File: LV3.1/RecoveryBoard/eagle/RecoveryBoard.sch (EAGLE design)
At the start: 90 parts, among them IC1 BD62120AEFJ-E2, Q6 MOSFET-PCH-SOT23-6, U1 STM32F042K6, U10 TPS63070, Y1 ECS-160-10-36Q-ES-TR

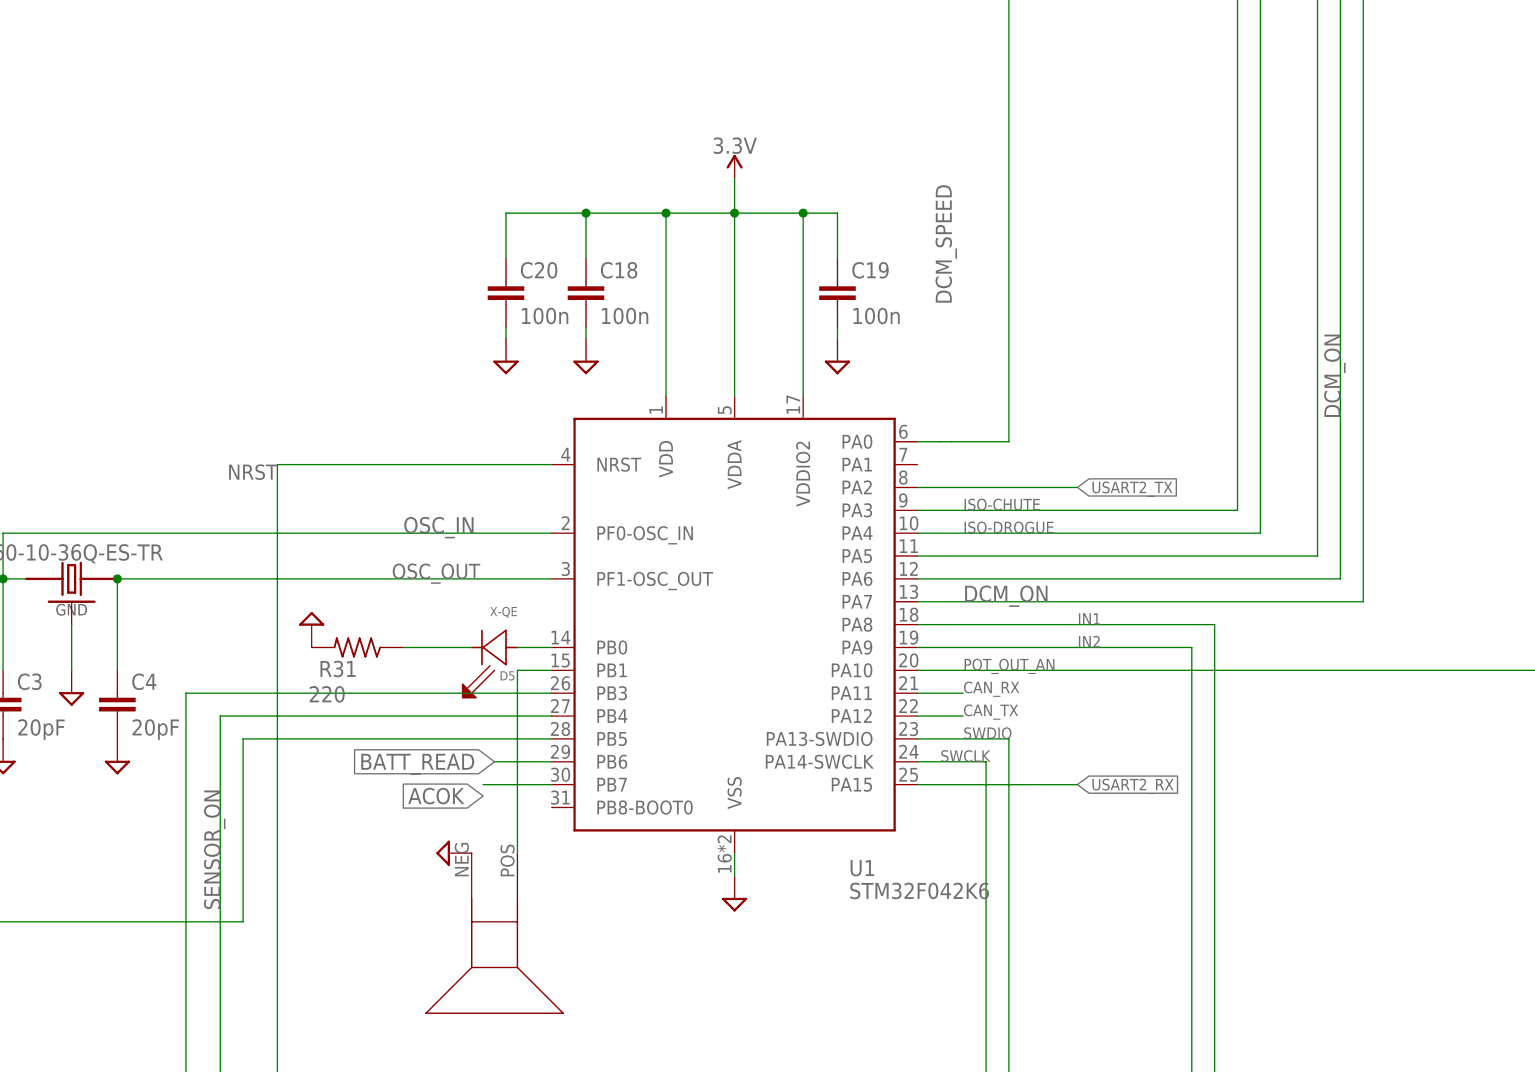
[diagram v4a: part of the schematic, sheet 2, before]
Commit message: finished routing and added TODO list
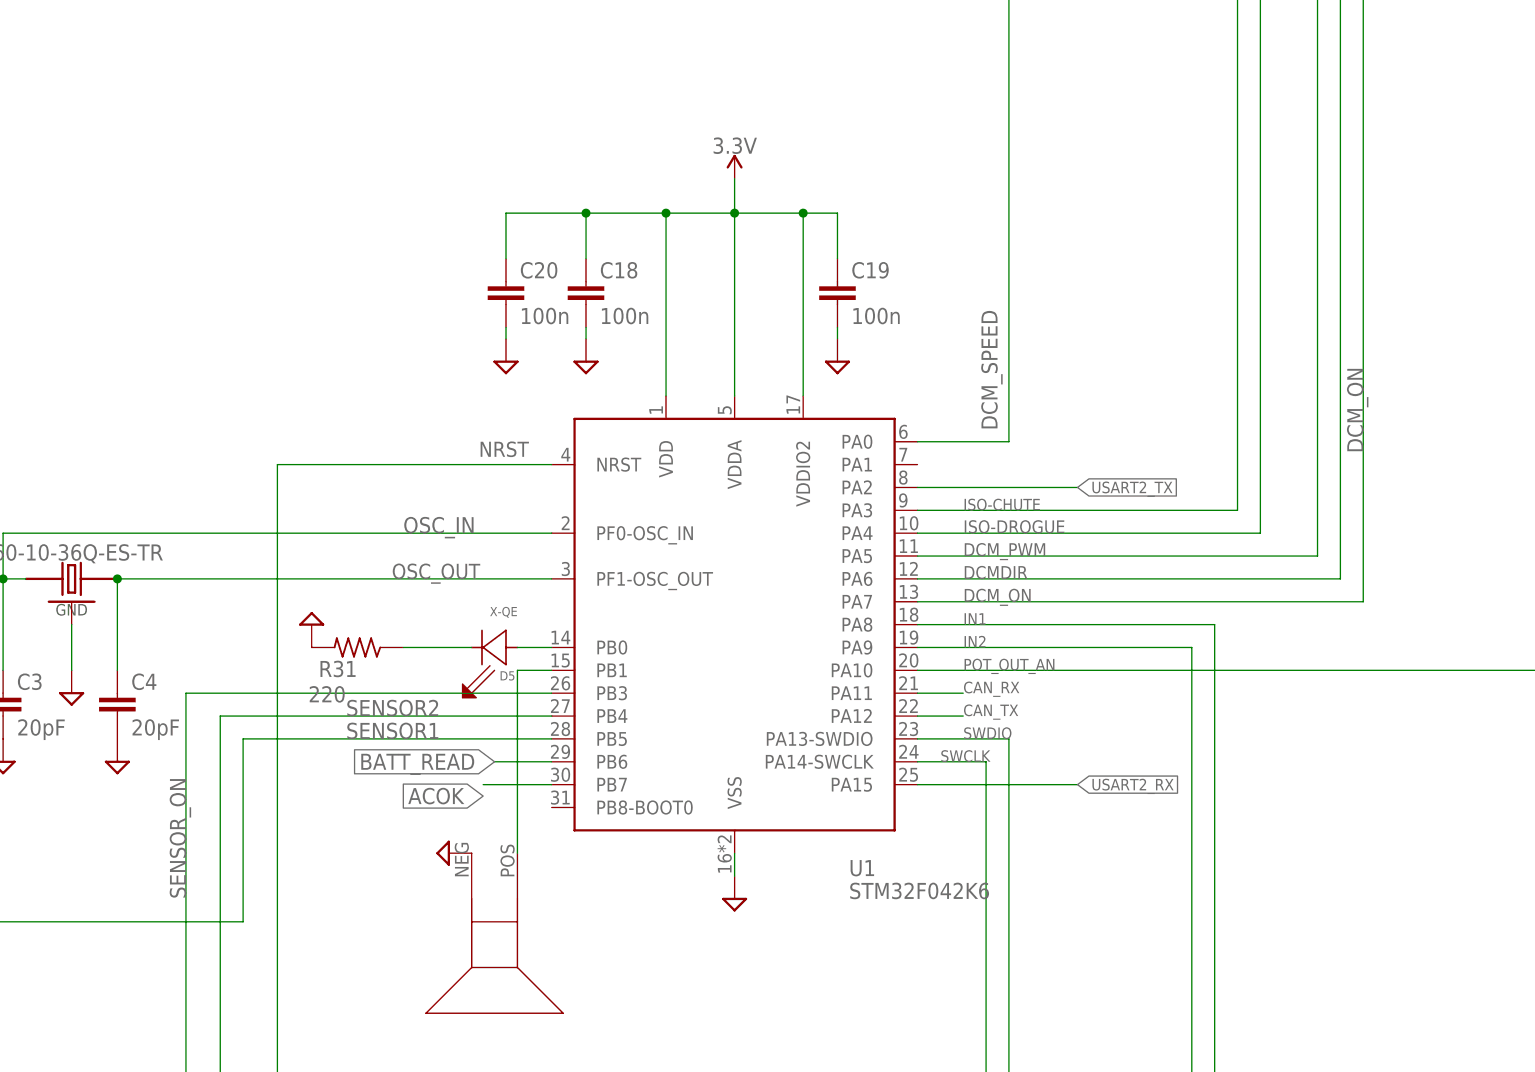
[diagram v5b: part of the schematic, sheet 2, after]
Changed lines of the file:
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@@
 <pinref part="U1" gate="G$1" pin="PA8"/>
 <wire x1="294.64" y1="185.42" x2="327.66" y2="185.42" width="0.1524" layer="91"/>
-<label x="312.42" y="185.42" size="1.27" layer="95"/>
+<label x="299.72" y="185.42" size="1.27" layer="95"/>
 <pinref part="R32" gate="R" pin="1"/>
 <junction x="386.08" y="118.11"/>
@@
 <pinref part="U1" gate="G$1" pin="PA9"/>
 <wire x1="294.64" y1="182.88" x2="325.12" y2="182.88" width="0.1524" layer="91"/>
-<label x="312.42" y="182.88" size="1.27" layer="95"/>
+<label x="299.72" y="182.88" size="1.27" layer="95"/>
 <wire x1="325.12" y1="182.88" x2="325.12" y2="134.62" width="0.1524" layer="91"/>
 <wire x1="325.12" y1="134.62" x2="386.08" y2="134.62" width="0.1524" layer="91"/>
@@
 <wire x1="219.71" y1="172.72" x2="219.71" y2="152.4" width="0.1524" layer="91"/>
 <wire x1="219.71" y1="172.72" x2="254" y2="172.72" width="0.1524" layer="91"/>
+<label x="231.14" y="172.72" size="1.778" layer="95"/>
 </segment>
 </net>
@@
 <pinref part="U1" gate="G$1" pin="NRST"/>
 <wire x1="254" y1="203.2" x2="223.52" y2="203.2" width="0.1524" layer="91"/>
-<label x="223.52" y="203.2" size="1.6764" layer="95" rot="R180"/>
+<label x="251.46" y="205.74" size="1.6764" layer="95" rot="R180"/>
 <pinref part="CM1" gate="A" pin="!RESET"/>
 <label x="251.46" y="48.26" size="1.6764" layer="95" rot="R180"/>
@@
 <pinref part="U1" gate="G$1" pin="PA6"/>
 <wire x1="294.64" y1="190.5" x2="341.63" y2="190.5" width="0.1524" layer="91"/>
+<label x="299.72" y="190.5" size="1.4224" layer="95"/>
 </segment>
 </net>
@@
 <wire x1="88.9" y1="95.25" x2="91.44" y2="95.25" width="0.1524" layer="91"/>
 <junction x="88.9" y="95.25"/>
-<label x="217.17" y="153.67" size="1.778" layer="95" rot="R90"/>
 <label x="130.81" y="76.2" size="1.778" layer="95"/>
 <pinref part="U1" gate="G$1" pin="PB3"/>
 <wire x1="213.36" y1="177.8" x2="254" y2="177.8" width="0.1524" layer="91"/>
+<label x="213.36" y="154.94" size="1.778" layer="95" rot="R90"/>
 </segment>
 </net>
@@
 <pinref part="U1" gate="G$1" pin="PB4"/>
 <wire x1="254" y1="175.26" x2="217.17" y2="175.26" width="0.1524" layer="91"/>
+<label x="231.14" y="175.26" size="1.778" layer="95"/>
 </segment>
 </net>
@@
 <wire x1="339.09" y1="193.04" x2="339.09" y2="269.24" width="0.1524" layer="91"/>
 <wire x1="339.09" y1="193.04" x2="294.64" y2="193.04" width="0.1524" layer="91"/>
+<label x="299.72" y="193.04" size="1.4224" layer="95"/>
 </segment>
 </net>
@@
 <wire x1="387.35" y1="261.62" x2="344.17" y2="261.62" width="0.1524" layer="91"/>
 <junction x="393.7" y="312.42"/>
-<label x="341.63" y="208.28" size="1.778" layer="95" rot="R90"/>
+<label x="344.17" y="204.47" size="1.778" layer="95" rot="R90"/>
 <wire x1="344.17" y1="261.62" x2="344.17" y2="187.96" width="0.1524" layer="91"/>
 <pinref part="U1" gate="G$1" pin="PA7"/>
-<label x="299.72" y="187.96" size="1.778" layer="95"/>
+<label x="299.72" y="187.96" size="1.4224" layer="95"/>
 <wire x1="294.64" y1="187.96" x2="344.17" y2="187.96" width="0.1524" layer="91"/>
 </segment>
@@
 <junction x="459.74" y="275.59"/>
 <pinref part="U1" gate="G$1" pin="PA0"/>
-<wire x1="298.45" y1="205.74" x2="297.18" y2="205.74" width="0.1524" layer="91"/>
-<label x="298.45" y="220.98" size="1.778" layer="95" rot="R90"/>
-<wire x1="297.18" y1="205.74" x2="294.64" y2="205.74" width="0.1524" layer="91"/>
+<label x="303.53" y="207.01" size="1.778" layer="95" rot="R90"/>
 <wire x1="304.8" y1="264.16" x2="304.8" y2="205.74" width="0.1524" layer="91"/>
-<wire x1="304.8" y1="205.74" x2="298.45" y2="205.74" width="0.1524" layer="91"/>
+<wire x1="304.8" y1="205.74" x2="294.64" y2="205.74" width="0.1524" layer="91"/>
 </segment>
 </net>
@@
 <net name="ISO-DROGUE" class="0">
 <segment>
-<label x="299.72" y="195.58" size="1.27" layer="95"/>
+<label x="299.72" y="195.58" size="1.4224" layer="95"/>
 <wire x1="332.74" y1="195.58" x2="332.74" y2="311.15" width="0.1524" layer="91"/>
 <wire x1="270.51" y1="311.15" x2="332.74" y2="311.15" width="0.1524" layer="91"/>

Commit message: More destruction on Ben's nice board. Good job Ben for putting up with Andrew.
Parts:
- removed U$1, U$2: NCH-SOT223, Q-MOSFET-NCH-SOT223:NCH-SOT223
- added Q1, Q2, Q3: BSS123, transistor-small-signal:BSS123
- added R37: 10k, oresat-rcl:R-US_0603-C-NOSILK
- D3, D4, D5: value X-QE -> (none); device D-Cree-XQE-LED:X-QE -> led:LEDCHIPLED_0603
- R18, R30: value (none) -> 1k
- R31: value 220 -> 1k
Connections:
- net N$9 renamed !BEN
- new net N$1: Q1.D, U$7.NEG
- net 3.3V: now also U$7.POS
- net DCM_ON: now also Q3.G; no longer U$1.G
- net GND: now also IC1.EP, Q1.S, Q2.S, Q3.S, R37.2; no longer U$1.S, U$2.S, U$7.NEG
- net N$27: now also Q2.D; no longer U$2.D
- net N$6: now also Q3.D; no longer U$1.D
- net N$8: now also Q1.G, R37.1; no longer U$7.POS
- net SENSOR_ON: now also Q2.G; no longer U$2.G
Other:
- note added: "From Telemetrum"
- note removed: "Do we still need an Arm input? there is no state where the board has power and is disarmed...this would free up a pin for a lock button"
- note removed: "Motor Control"
- moved on the sheet: C11, C12, C13, C14, C15, C16, C17, C21, D1, D2, JP1, JP2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

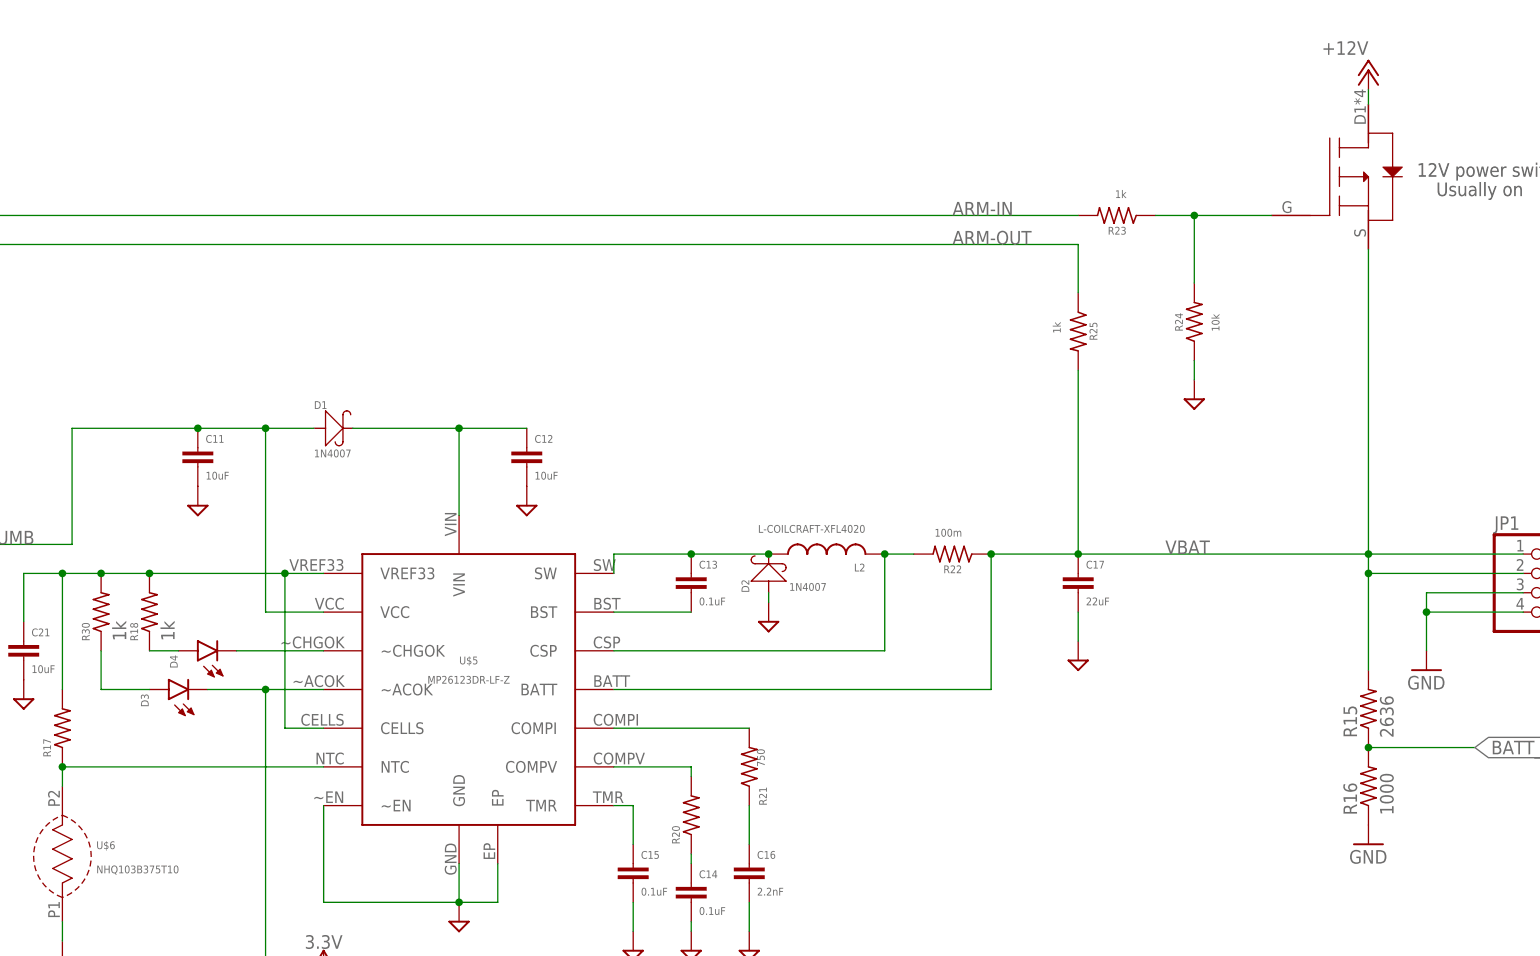
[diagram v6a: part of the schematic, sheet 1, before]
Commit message: edited board after design meeting on 1/15
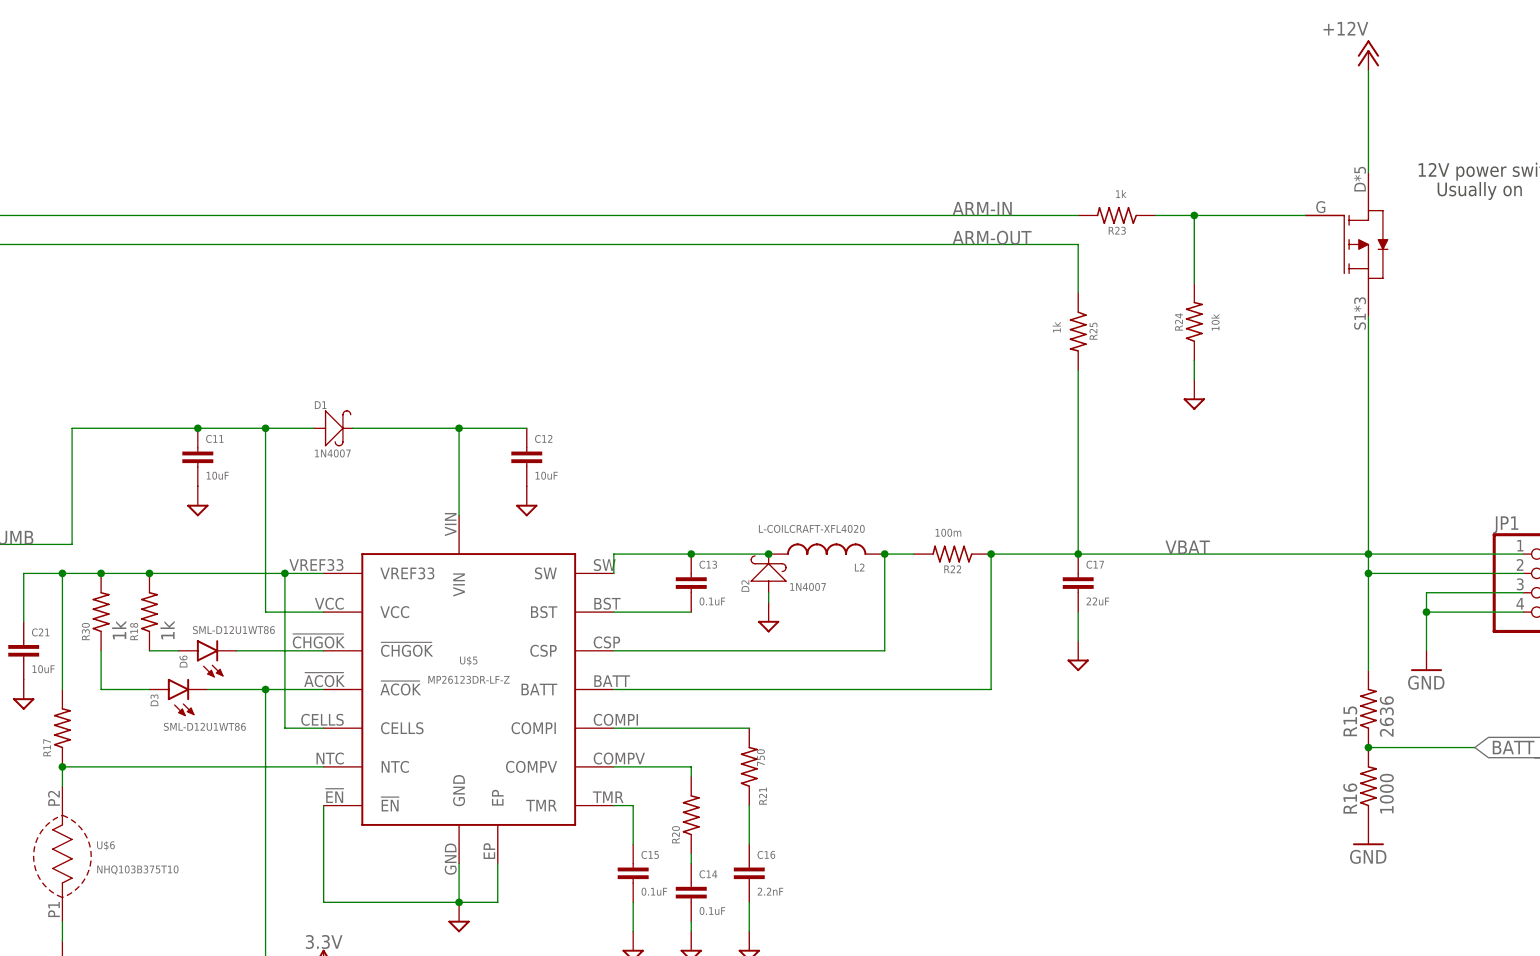
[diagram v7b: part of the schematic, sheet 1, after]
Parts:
- D3, D5, D6: value (none) -> SML-D12U1WT86; DIS (none) -> Digikey; DPN (none) -> SML-D12U1WT86CT-ND; MPN (none) -> SML-D12U1WT86
- R26: value TBD -> 50
- R28: value 10k -> 50
- U$8: value AO6405 -> SI7465DP; device Q--AO6405--P-CH MOSFET for Arm Switch:AO6405 -> Q--Si7465DP--Vishay Power MOSFET with multple S+D leads:SI7465DP
- renumbered D4 to D6
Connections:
- net N$15 renamed LED
- net N$8 renamed SPKR
- net ACOK: now also U$5.!ACOK; no longer U$5.~ACOK
- net GND: now also U$5.!EN; no longer U$5.~EN
- net N$13: now also U$5.!CHGOK; no longer U$5.~CHGOK
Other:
- moved on the sheet: U$5
